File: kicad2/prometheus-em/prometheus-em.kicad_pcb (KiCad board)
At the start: 2 copper layers, 42 x 40 mm, 78 parts, among them IC1 RP2040, IC2 SIT2001BI-S2-33E-12.000000G, IC3 W25Q128JVSIQ, IC4 TB67H450FNG,EL, IC5 TB67H450FNG,EL, IC6 PCA9306YZTR, IC7 S-89431ACMC-HBVT2U, IC8 NJM2884U1-33-TE1, J1 MOE_A, J2 GNSS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

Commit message: update pcb
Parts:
- IC4, IC5, J5, J6, J7: moved to B.Cu
- moved J5 91.3 mm to (43.0, 38.0), turned to 90 degrees
- moved J7 88.2 mm to (45.0, 69.4), turned to 180 degrees
- moved Q3 85.6 mm to (50.8, 70.2), turned to 180 degrees
- moved IC4 79.5 mm to (42.0, 44.0), turned to 90 degrees
- moved S3 79.2 mm to (43.2, 73.5)
- moved IC8 74.5 mm to (44.0, 64.0)
- moved R22 55.0 mm to (50.0, 74.0)
- moved J8 53.7 mm to (94.0, 84.0)
- moved R23 51.9 mm to (50.0, 73.0), turned to 180 degrees
- moved IC1 51.6 mm to (58.5, 55.6), turned to 180 degrees
- moved IC3 50.5 mm to (66.8, 63.9), turned to 180 degrees
- moved J6 44.7 mm to (73.4, 37.9), turned to 90 degrees
- moved U2 43.3 mm to (52.0, 48.6)
- moved IC5 38.3 mm to (72.0, 44.0), turned to 90 degrees
- moved J4 23.0 mm to (73.0, 52.0)
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
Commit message: complete prometheus-em pcb
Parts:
- added C22: 1u, Capacitor_SMD:C_0402_1005Metric, F.Cu at (51.7, 39.6)
- added C23: 1u, Capacitor_SMD:C_0402_1005Metric, F.Cu at (58.8, 40.1)
- added C24: 1u, Capacitor_SMD:C_0402_1005Metric, F.Cu at (41.8, 45.5)
- added C25: 1u, Capacitor_SMD:C_0402_1005Metric, F.Cu at (47.6, 46.2)
- added C26: 100u, Capacitor_SMD:C_1206_3216Metric, F.Cu at (73.9, 39.5)
- added D4: 1N4148W, Diode_SMD:D_SOD-123, F.Cu at (46.1, 62.1)
- added D5: LED, LED_SMD:LED_0603_1608Metric, F.Cu at (66.5, 46.4)
- added IC10: NJM2878F3-33-TE2, SamacSys_Parts:SOT65P210X100-5N, F.Cu at (44.6, 45.6)
- added IC9: NJM12888F33-TE1, SamacSys_Parts:SOT95P280X130-5N, F.Cu at (55.2, 40.6)
- added R30: 10k, Resistor_SMD:R_0402_1005Metric, F.Cu at (64.1, 45.7)
- added R31: 1k, Resistor_SMD:R_0402_1005Metric, F.Cu at (66.5, 49.3)
- C1, C10, C2, C5, C6: footprint Capacitor_SMD:C_0402_1005Metric -> Capacitor_SMD:C_0603_1608Metric; moved to B.Cu
- C8, C9: value 2.2u -> 1u
- R17: moved to B.Cu
- U2: value ICM-20948 -> ICM-20948-SL
- moved U3 110.2 mm to (43.6, 65.7), turned to 180 degrees
- moved R28 105.4 mm to (47.9, 56.5), turned to -90 degrees
- moved R25 102.4 mm to (50.8, 68.8)
- moved C20 100.6 mm to (44.2, 49.1)
- moved R27 99.9 mm to (42.5, 52.2), turned to 90 degrees
- moved C10 99.1 mm to (58.5, 61.7), turned to -90 degrees
- moved R13 99.0 mm to (39.8, 50.5), turned to -90 degrees
- moved R11 98.9 mm to (39.8, 42.9), turned to -90 degrees
- moved R9 98.8 mm to (57.7, 43.4)
- moved IC7 97.2 mm to (50.4, 65.5), turned to 90 degrees
- moved C5 96.6 mm to (60.5, 49.4), turned to 180 degrees
- moved R17 95.9 mm to (50.3, 66.7)
- moved R12 92.9 mm to (60.5, 43.4)
- moved R26 92.3 mm to (55.1, 62.7)
- moved R24 91.4 mm to (46.9, 41.0), turned to 90 degrees
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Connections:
- C15 pad 1: /7V4 -> Net-(C15-Pad1)
- D2 pad 1: /7V4 -> Net-(C15-Pad1)
- IC1 pad 11: unconnected-(IC1-Pad11) -> /GPIO8_ToF_SDA
- IC1 pad 12: unconnected-(IC1-Pad12) -> /GPIO9_ToF_SCL
- IC1 pad 13: /GPIO10_MO_A1 -> unconnected-(IC1-Pad13)
- IC1 pad 14: /GPIO11_MO_A2 -> /GPIO14_ToF_RST
- IC1 pad 15: /GPIO12_IMU_SDA -> /GPIO12_LED
- IC1 pad 16: /GPIO13_IMU_SCL -> /GPIO13_LED
- IC1 pad 17: unconnected-(IC1-Pad17) -> /GPIO14_IMU_SDA
- IC1 pad 18: unconnected-(IC1-Pad18) -> /GPIO15_IMU_SCL
- IC1 pad 26: unconnected-(IC1-Pad26) -> /RUN
- IC1 pad 28: unconnected-(IC1-Pad28) -> /GPIO17_Nichrome
- IC1 pad 31: /GPIO20_MOE_A1 -> /GPIO20_MO_A1
- IC1 pad 32: /GPIO21_MOE_B1 -> /GPIO21_MO_A2
- IC1 pad 34: /GPIO22_MOE_A2 -> /GPIO22_MOE_A1
- IC1 pad 35: /GPIO23_MOE_B2 -> /GPIO23_MOE_B1
- IC1 pad 36: /GPIO24_Nichrome -> /GPIO24_MOE_A2
- IC1 pad 37: /GPIO25_LED -> /GPIO25_MOE_B2
- IC1 pad 38: /GPIO26_Imonitor -> unconnected-(IC1-Pad38)
- IC1 pad 40: unconnected-(IC1-Pad40) -> /GPIO28_Imonitor
- IC1 pad 5: /GPIO3_ToF_RST -> unconnected-(IC1-Pad5)
- IC1 pad 8: /GPIO6_ToF_SDA -> unconnected-(IC1-Pad8)
- IC1 pad 9: /GPIO7_ToF_SCL -> unconnected-(IC1-Pad9)
- IC4 pad 2: /GPIO11_MO_A2 -> /GPIO20_MO_A1
- IC4 pad 3: /GPIO10_MO_A1 -> /GPIO21_MO_A2
- IC4 pad 4: +3V3 -> /3V3A
- IC4 pad 9: unconnected-(IC4-Pad9) -> GND
- IC5 pad 2: /GPIO19_MO_B2 -> /GPIO18_MO_B1
- IC5 pad 3: /GPIO18_MO_B1 -> /GPIO19_MO_B2
- IC5 pad 4: +3V3 -> /3V3A
- IC5 pad 9: unconnected-(IC5-Pad9) -> GND
- IC6 pad C2: /GPIO13_IMU_SCL -> /GPIO15_IMU_SCL
- IC6 pad D2: /GPIO12_IMU_SDA -> /GPIO14_IMU_SDA
- IC7 pad 3: /GPIO26_Imonitor -> /GPIO28_Imonitor
- IC7 pad 4: /GPIO26_Imonitor -> /GPIO28_Imonitor
- IC8 pad 6: /7V4 -> Net-(C15-Pad1)
- J1 pad 2: /GPIO20_MOE_A1 -> /GPIO22_MOE_A1
- J1 pad 3: /GPIO22_MOE_A2 -> /GPIO24_MOE_A2
- J2 pad 2: /GPIO4_GNSS_TX -> /GPIO5_GNSS_RX
- J2 pad 3: /GPIO5_GNSS_RX -> /GPIO4_GNSS_TX
- J3 pad 2: /GPIO21_MOE_B1 -> /GPIO23_MOE_B1
- J3 pad 3: /GPIO23_MOE_B2 -> /GPIO25_MOE_B2
- J4 pad 1: /GPIO7_ToF_SCL -> /GPIO14_ToF_RST
- J4 pad 2: /GPIO3_ToF_RST -> /GPIO9_ToF_SCL
- J4 pad 3: /GPIO6_ToF_SDA -> /GPIO8_ToF_SDA
- R15 pad 2: /GPIO13_IMU_SCL -> /GPIO15_IMU_SCL
- R16 pad 2: /GPIO12_IMU_SDA -> /GPIO14_IMU_SDA
- R21 pad 1: /GPIO24_Nichrome -> /GPIO17_Nichrome
- R7 pad 1: /GPIO25_LED -> /GPIO12_LED
- U2 pad 5: GND -> Net-(U2-Pad5)
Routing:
- net +3V3: track 0.00 -> 205.5 mm, vias 0 -> 20
- net GND: track 0.00 -> 126.8 mm, vias 0 -> 168
- net /7V4: track 0.00 -> 101.4 mm, vias 0 -> 16
- net +1V8: track 0.00 -> 28.4 mm, vias 0 -> 1
- net Net-(C15-Pad1): track 0.00 -> 23.5 mm, vias 0 -> 2
- net /QSPI_SS: track 0.00 -> 20.1 mm
- net /GPIO18_MO_B1: track 0.00 -> 18.7 mm, vias 0 -> 1
- net /GPIO19_MO_B2: track 0.00 -> 18.4 mm, vias 0 -> 1
- net /BAT_IN: track 0.00 -> 18.0 mm
- net +1V1: track 0.00 -> 17.7 mm, vias 0 -> 4
- net /GPIO17_Nichrome: track 0.00 -> 17.1 mm
- net /QSPI_SD1: track 0.00 -> 16.4 mm
- net /VBUS: track 0.00 -> 14.3 mm
- net /GPIO20_MO_A1: track 0.00 -> 13.9 mm, vias 0 -> 1
- net /GPIO15_IMU_SCL: track 0.00 -> 13.8 mm
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- added copper zone on F.Cu, net +1V1
- added copper zone on F.Cu, net +3V3
- added copper zone on B.Cu, net GND
- added copper zone on F.Cu, net GND
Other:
- board text added: "1"
- board text added: "2"
- board text added: "2022.11 Akio M"
- board text added: "3V3"
- board text added: "A"
- board text added: "B"
- board text added: "BOOT"
- board text added: "CanSat"
- board text added: "DERC"
- board text added: "GND"
- board text added: "GNSS"
- board text added: "Heat"
- board text added: "JST PH-3"
- board text added: "ME-A"
- board text added: "ME-B"
- board text added: "Motor2"
- board text added: "PWR"
- board text added: "Prometheus"
- board text added: "RST"
- board text added: "RUN"
- board text added: "RX"
- board text added: "SCL"
- board text added: "SDA"
- board text added: "TX"
- board text added: "ToF"
- board text added: "←"
- board text added: "→"

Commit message: update kicad pcb
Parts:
- C1, C2: footprint Capacitor_SMD:C_0603_1608Metric -> Capacitor_SMD:C_0402_1005Metric; moved to F.Cu
- J1, J3: footprint tanekonsat:PinHeader_1x04_P2.00mm_Vertical -> Connector_PinHeader_2.00mm:PinHeader_1x04_P2.00mm_Vertical
- J2: footprint tanekonsat:PinHeader_1x04_P2.00mm_Vertical -> Connector_JST_ZH:JST_ZH_B4B-ZR_1x04_P1.50mm_Vertical
- J4: footprint tanekonsat:PinHeader_1x05_P2.00mm_Vertical -> Connector_JST_ZH:JST_ZH_B5B-ZR_1x05_P1.50mm_Vertical
- J8: footprint tanekonsat:PinHeader_1x02_P2.00mm_Vertical -> Connector_PinHeader_2.00mm:PinHeader_1x02_P2.00mm_Vertical
- S1, S2: value SKRPABE010 -> SKRPACE010; footprint SamacSys_Parts:SKRPABE010 -> SamacSys_Parts:SMT_4.2X3.2_
- moved J4 5.48 mm to (73.1, 43.9), turned to -90 degrees
- moved J2 4.11 mm to (73.1, 53.9), turned to -90 degrees
- moved C2 0.91 mm to (68.8, 55.0)
- moved R14 0.90 mm to (40.5, 40.0), turned to 0 degrees
- moved C1 0.39 mm to (68.8, 58.2)
- moved C17 0.28 mm to (70.7, 39.2)
- moved C19 0.25 mm to (67.3, 39.2)
- moved C26 0.25 mm to (73.9, 39.2)
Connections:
- IC4 pad 9: GND -> unconnected-(IC4-Pad9)
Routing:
- net +3V3: track 205.5 -> 196.0 mm, vias 20 -> 16
- net GND: track 126.8 -> 136.3 mm, vias 168 -> 187
- net /GPIO8_ToF_SDA: track 7.41 -> 11.7 mm, vias 2 -> 0
- net /GPIO9_ToF_SCL: track 8.02 -> 12.2 mm, vias 2 -> 0
- net /GPIO14_ToF_RST: track 8.95 -> 12.3 mm
- net /GPIO4_GNSS_TX: track 3.51 -> 6.67 mm
- net /7V4: track 101.4 -> 99.0 mm, vias 16 -> 15
- net /GPIO5_GNSS_RX: track 4.32 -> 6.58 mm

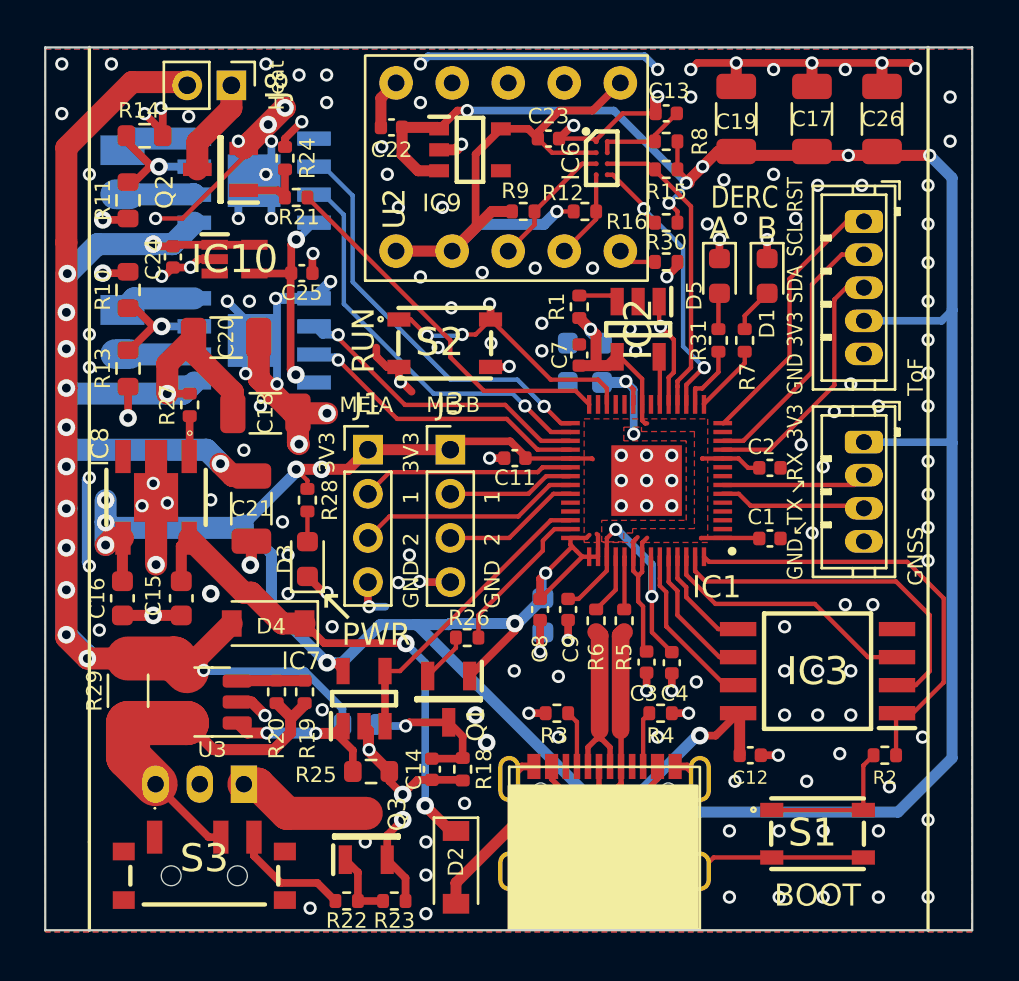
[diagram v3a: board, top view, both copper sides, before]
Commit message: add gnss-board rev2 and main-board rev3
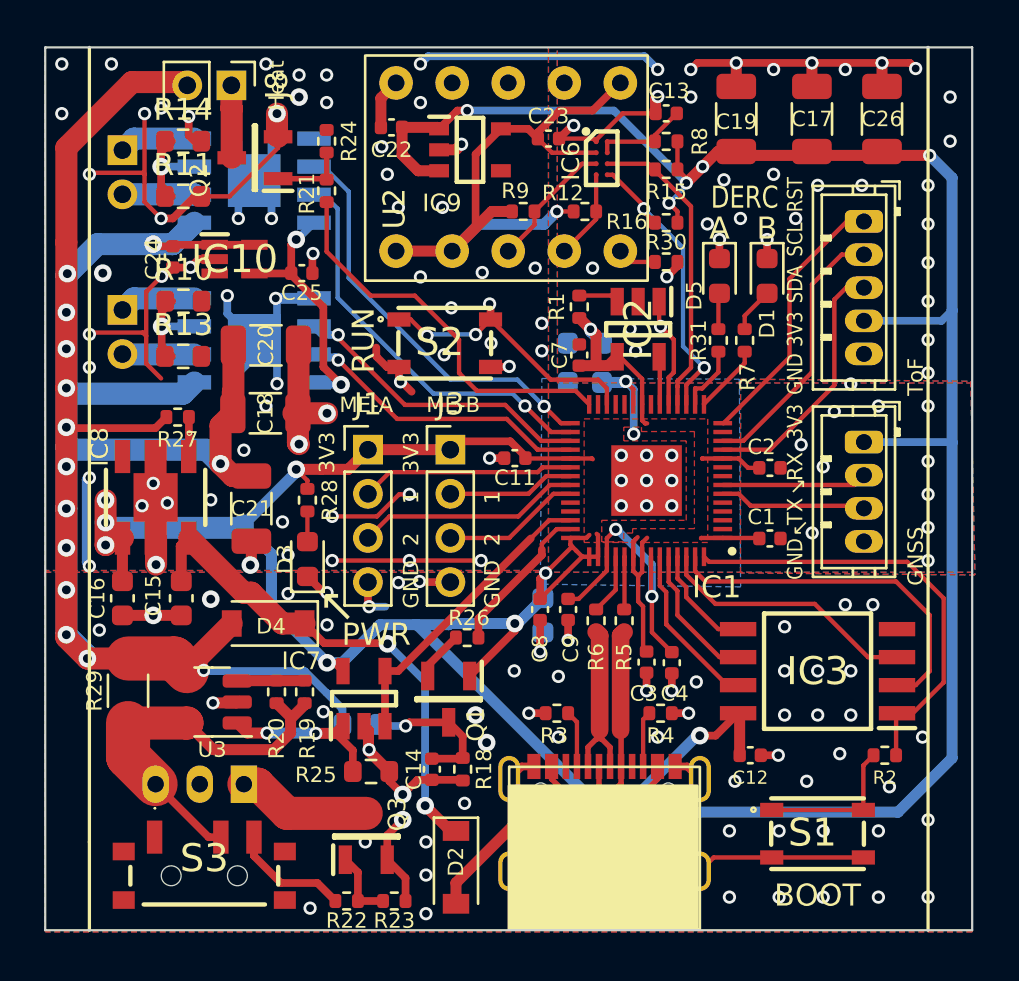
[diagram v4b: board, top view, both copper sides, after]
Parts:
- J5, J6: footprint tanekonsat:PinHeader_1x02_P2.00mm_Vertical -> Connector_PinHeader_2.00mm:PinHeader_1x02_P2.00mm_Vertical
- R10, R11, R13, R14: value R -> 1
- moved R10 2.56 mm to (42.3, 47.5), turned to 0 degrees
- moved R13 2.56 mm to (42.2, 50.0), turned to 0 degrees
- moved R11 2.51 mm to (42.2, 42.8), turned to 0 degrees
- moved R24 2.04 mm to (48.8, 40.2)
- moved C20 1.84 mm to (46.0, 49.5)
- moved R14 1.77 mm to (42.2, 40.2)
- moved Q2 1.65 mm to (45.5, 41.0)
- moved R21 1.41 mm to (48.8, 42.5), turned to 90 degrees
- moved R27 0.78 mm to (42.0, 52.8), turned to 180 degrees
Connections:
- IC4 pad 9: unconnected-(IC4-Pad9) -> GND
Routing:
- net GND: track 136.3 -> 154.6 mm, vias 187 -> 182
- net /7V4: track 99.0 -> 102.3 mm, vias 15 -> 14
- net /3V3A: track 10.1 -> 11.7 mm
- net Net-(J8-Pad1): track 4.45 -> 3.29 mm
- net /GPIO17_Nichrome: track 17.1 -> 17.9 mm
- net Net-(IC5-Pad7): track 5.14 -> 4.41 mm
- net Net-(IC4-Pad7): track 4.94 -> 4.37 mm
- net +3V3: track 196.0 -> 195.9 mm, vias 16 -> 14
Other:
- board text added: "DERC Cansat Project Prometheus Main Board -rev.3 Design: Akio M 2022.12"
- board text removed: "2022.11 Akio M"

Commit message: update sch & pcb (em-rev4!)
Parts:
- removed R23, R26: 10k, Resistor_SMD:R_0402_1005Metric
- IC6: value PCA9306YZTR -> PCA9306DCUR; footprint SamacSys_Parts:BGA8C50P2X4_89X189X62 -> SamacSys_Parts:SOP50P310X90-8N
- Q3: value IRFML8244TRPBF -> IRLML6402
- R10, R11, R13, R14: footprint Resistor_SMD:R_0603_1608Metric -> Resistor_SMD:R_0402_1005Metric
- R22: value 10k -> 100k
- moved Q3 9.69 mm to (40.9, 72.7), turned to 180 degrees
- moved R9 8.37 mm to (65.6, 40.8), turned to -90 degrees
- moved R22 6.73 mm to (47.5, 68.3)
- moved R15 5.37 mm to (58.8, 42.1)
- moved S3 5.09 mm to (48.3, 73.5)
- moved R16 3.87 mm to (60.3, 43.4)
- moved R12 3.06 mm to (63.5, 43.7)
- moved C13 1.37 mm to (62.8, 39.3)
- moved R8 1.29 mm to (65.0, 39.3)
- moved IC6 1.25 mm to (62.4, 41.4)
- moved J4 1.20 mm to (71.9, 43.8)
- moved J2 1.19 mm to (71.9, 53.9)
- moved D1 0.71 mm to (68.0, 46.3)
- moved C1 0.56 mm to (68.5, 57.8), turned to 90 degrees
- moved C2 0.42 mm to (68.5, 54.8), turned to -90 degrees
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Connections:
- C15 pad 1: Net-(C15-Pad1) -> /VREG
- D2 pad 1: Net-(C15-Pad1) -> /VREG
- D4 pad 1: Net-(C15-Pad1) -> /VREG
- IC8 pad 6: Net-(C15-Pad1) -> /VREG
- J7 pad 1: GNDA -> /BAT_IN
- J7 pad 3: /BAT_IN -> GND
- Q1 pad 2: Net-(Q1-Pad2) -> /GPIO29_Vmonitor
- Q3 pad 1: Net-(Q3-Pad1) -> Net-(S3-Pad2)
- Q3 pad 2: GND -> /BAT_IN
- Q3 pad 3: GNDA -> /7V4
- R12 pad 1: +1V8 -> +3V3
- R12 pad 2: /IMU_SDA -> /GPIO14_IMU_SDA
- R15 pad 1: +3V3 -> /IMU_SCL
- R15 pad 2: /GPIO15_IMU_SCL -> +1V8
- R16 pad 1: +3V3 -> /IMU_SDA
- R16 pad 2: /GPIO14_IMU_SDA -> +1V8
- R22 pad 1: Net-(R22-Pad1) -> /BAT_IN
- R22 pad 2: Net-(Q3-Pad1) -> Net-(S3-Pad2)
- R27 pad 2: /7V4 -> /VREG
- R9 pad 1: +1V8 -> +3V3
- R9 pad 2: /IMU_SCL -> /GPIO15_IMU_SCL
- S3 pad 2: /BAT_IN -> Net-(S3-Pad2)
- S3 pad 3: Net-(R22-Pad1) -> GND
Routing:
- net /VREG: track 0.00 -> 29.3 mm, vias 0 -> 2
- net Net-(C15-Pad1): track 23.0 -> 0.00 mm, vias 2 -> 0
- net Net-(S3-Pad2): track 0.00 -> 13.0 mm
- net GNDA: track 6.09 -> 0.00 mm
- net Net-(R22-Pad1): track 5.39 -> 0.00 mm
- net +3V3: track 195.9 -> 199.7 mm, vias 14 -> 13
- net GND: track 154.6 -> 158.2 mm, vias 182 -> 184
- net +1V8: track 28.4 -> 24.9 mm, vias 1 -> 2
- net /7V4: track 102.3 -> 105.7 mm
- net Net-(Q3-Pad1): track 3.25 -> 0.00 mm
- net /GPIO29_Vmonitor: track 7.00 -> 9.70 mm
- net Net-(Q1-Pad2): track 2.27 -> 0.00 mm
- net /GPIO14_IMU_SDA: track 13.6 -> 12.2 mm
- net /GPIO8_ToF_SDA: track 11.7 -> 10.4 mm
- net /GPIO5_GNSS_RX: track 6.58 -> 5.40 mm
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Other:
- board text added: "Motor1"
- board text removed: "CanSat"
- board text removed: "Prometheus"

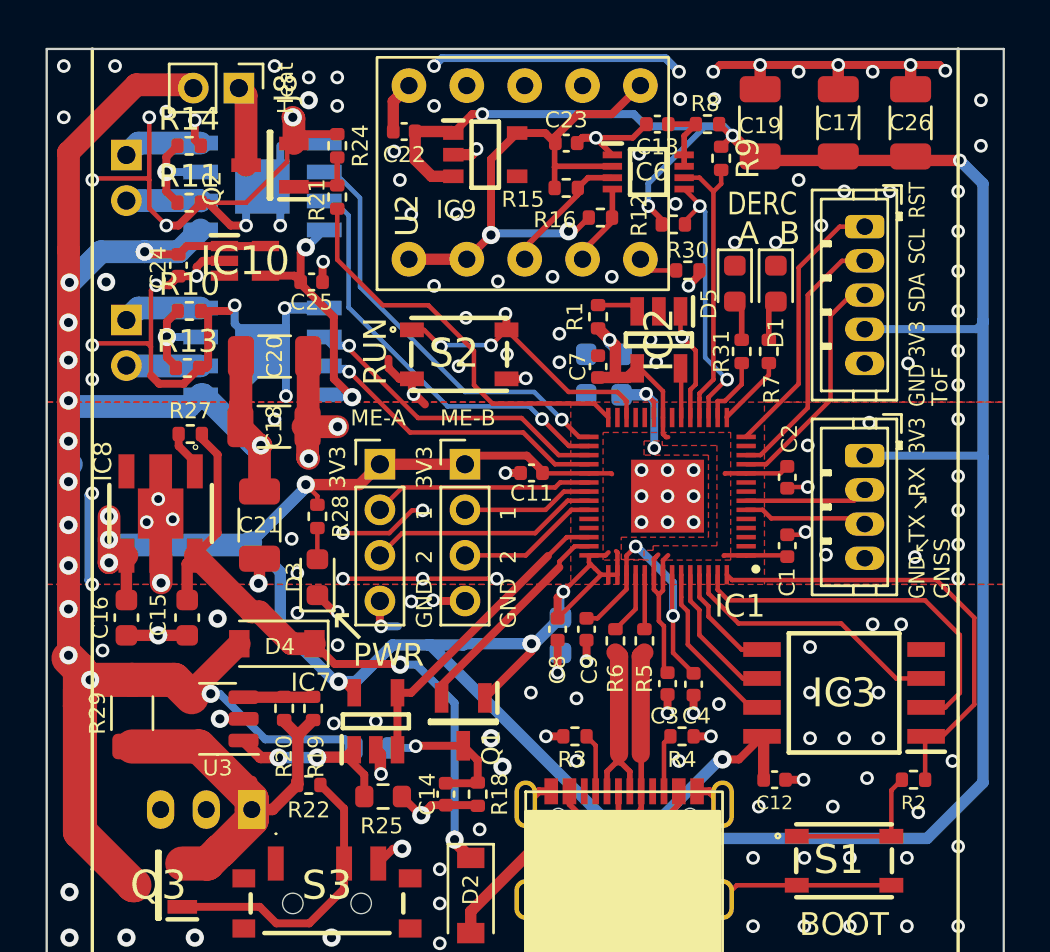
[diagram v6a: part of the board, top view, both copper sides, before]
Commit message: update main board pcb, add ublox-m10s pcb
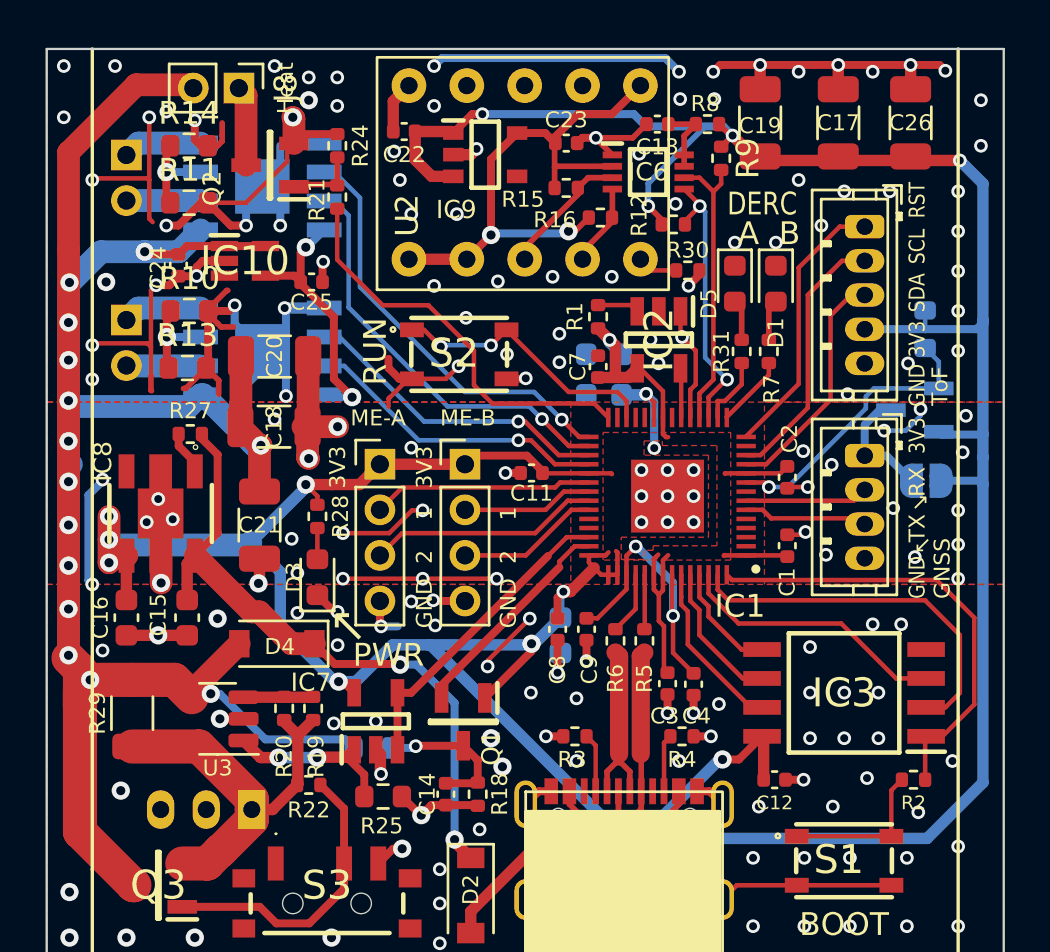
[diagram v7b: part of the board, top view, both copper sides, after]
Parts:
- added JP1: GNSS_Power_Jumper, Jumper:SolderJumper-2_P1.3mm_Open_RoundedPad1.0x1.5mm, B.Cu at (74.6, 55.0)
- added Q4: IRLML6402, SamacSys_Parts:SOT95P237X112-3N, B.Cu at (74.1, 51.9)
- added R23: 30k, Resistor_SMD:R_0603_1608Metric, B.Cu at (74.5, 48.3)
- R10, R11, R13, R14: footprint Resistor_SMD:R_0402_1005Metric -> Resistor_SMD:R_0603_1608Metric
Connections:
- IC1 pad 9: unconnected-(IC1-Pad9) -> /GPIO7_GNSS_RST
- J2 pad 1: +3V3 -> Net-(J2-Pad1)
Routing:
- net GND: track 158.2 -> 171.0 mm, vias 184 -> 191
- net /GPIO7_GNSS_RST: track 0.00 -> 12.7 mm, vias 0 -> 1
- net Net-(J2-Pad1): track 0.00 -> 5.27 mm
- net +3V3: track 199.7 -> 196.7 mm
- net Net-(IC5-Pad7): track 4.41 -> 3.02 mm
- net Net-(IC4-Pad7): track 4.37 -> 3.04 mm
- net /BAT_IN: track 18.7 -> 17.4 mm
- net /RUN: track 12.8 -> 12.1 mm, vias 3 -> 2
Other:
- board text added: "DERC Cansat Project Prometheus Main Board -rev.3a Design: Akio M 2022.12"
- board text removed: "DERC Cansat Project Prometheus Main Board -rev.3 Design: Akio M 2022.12"
